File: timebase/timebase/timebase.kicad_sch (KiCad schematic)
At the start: 59 parts

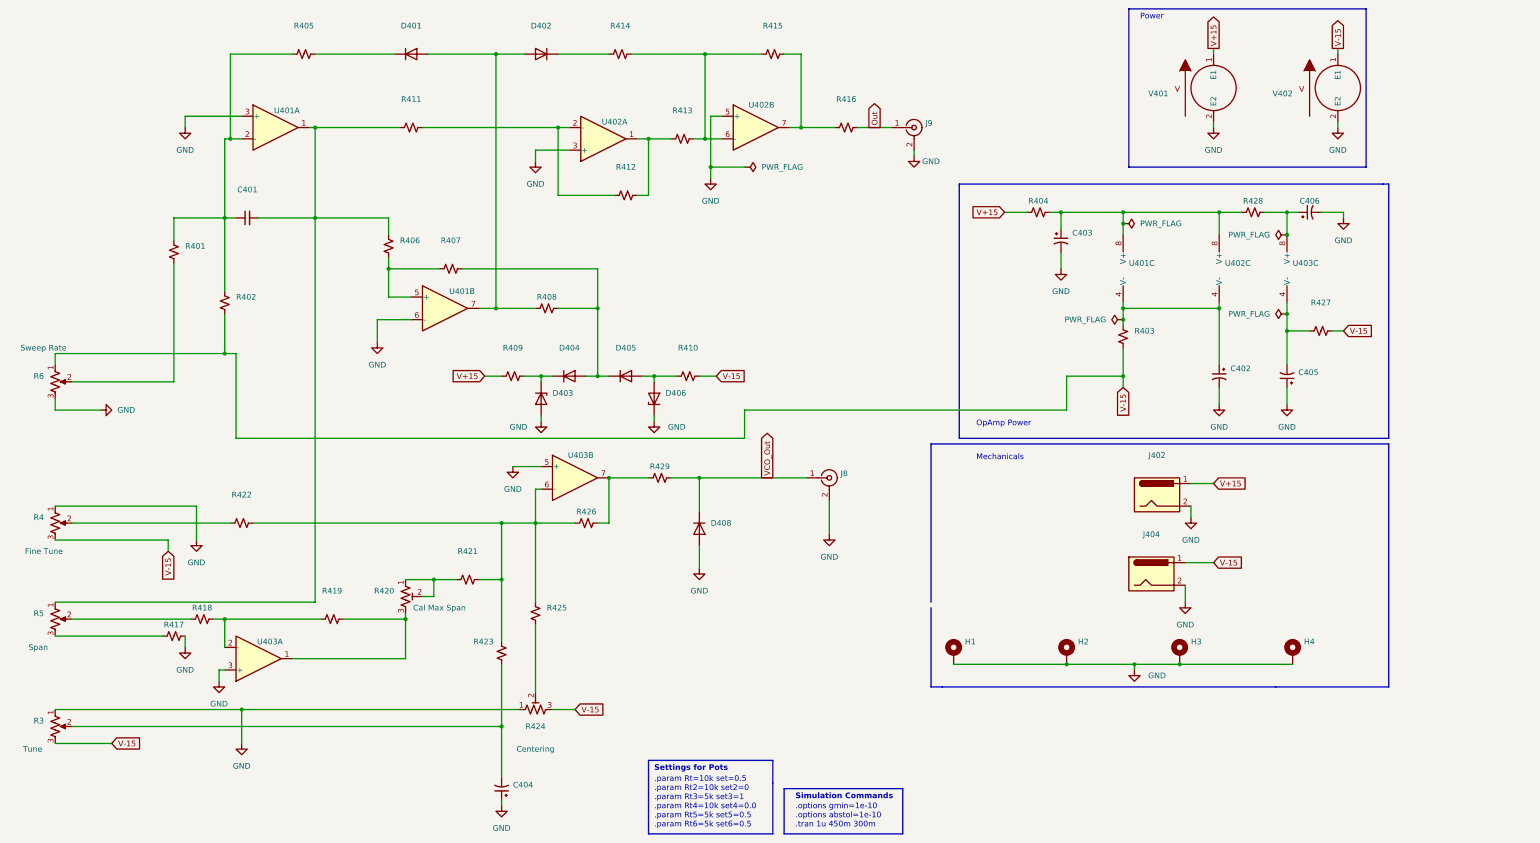
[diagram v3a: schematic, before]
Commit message: resolution-filters update
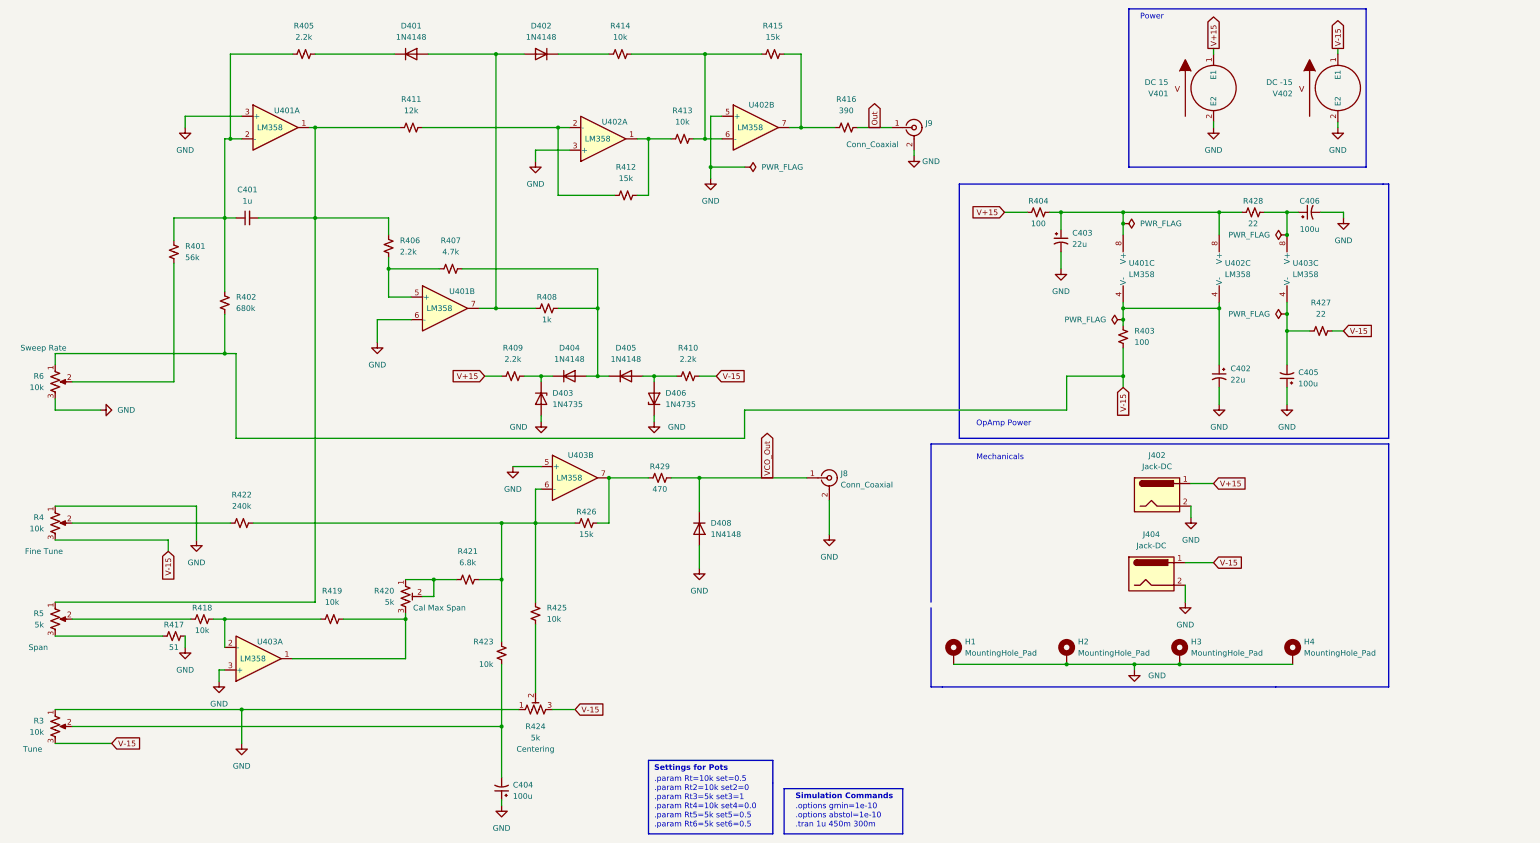
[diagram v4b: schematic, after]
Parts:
- C401: value (none) -> 1u; footprint (none) -> Capacitor_THT:C_Radial_D4.0mm_H5.0mm_P1.50mm
- C402, C403: value (none) -> 22u; footprint (none) -> Capacitor_THT:CP_Axial_L11.0mm_D6.0mm_P18.00mm_Horizontal
- C404, C405, C406: value (none) -> 100u; footprint (none) -> Capacitor_THT:CP_Axial_L11.0mm_D6.0mm_P18.00mm_Horizontal
- D401, D402, D404, D405, D408: value (none) -> 1N4148; footprint (none) -> Diode_THT:D_DO-35_SOD27_P7.62mm_Horizontal
- D403, D406: value (none) -> 1N4735; footprint (none) -> Diode_THT:D_DO-35_SOD27_P7.62mm_Horizontal
- H1, H2, H3, H4: value (none) -> MountingHole_Pad; footprint (none) -> MountingHole:MountingHole_2.7mm_M2.5_DIN965_Pad_TopOnly
- J402, J404: value (none) -> Jack-DC; footprint (none) -> timebase:CUI_PJ-007
- J8, J9: value (none) -> Conn_Coaxial; footprint (none) -> timebase:TE_5-1634503-1
- R3, R4, R6: value (none) -> 10k; footprint (none) -> Connector_Wire:SolderWire-0.127sqmm_1x03_P3.7mm_D0.48mm_OD1mm
- R401: value (none) -> 56k; footprint (none) -> Resistor_THT:R_Axial_DIN0207_L6.3mm_D2.5mm_P7.62mm_Horizontal
- R402: value (none) -> 680k; footprint (none) -> Resistor_THT:R_Axial_DIN0207_L6.3mm_D2.5mm_P7.62mm_Horizontal
- R403, R404: value (none) -> 100; footprint (none) -> Resistor_THT:R_Axial_DIN0207_L6.3mm_D2.5mm_P7.62mm_Horizontal
- R405, R406, R409, R410: value (none) -> 2.2k; footprint (none) -> Resistor_THT:R_Axial_DIN0207_L6.3mm_D2.5mm_P7.62mm_Horizontal
- R407: value (none) -> 4.7k; footprint (none) -> Resistor_THT:R_Axial_DIN0207_L6.3mm_D2.5mm_P7.62mm_Horizontal
- R408: value (none) -> 1k; footprint (none) -> Resistor_THT:R_Axial_DIN0207_L6.3mm_D2.5mm_P7.62mm_Horizontal
- R411: value (none) -> 12k; footprint (none) -> Resistor_THT:R_Axial_DIN0207_L6.3mm_D2.5mm_P7.62mm_Horizontal
- R412, R415, R426: value (none) -> 15k; footprint (none) -> Resistor_THT:R_Axial_DIN0207_L6.3mm_D2.5mm_P7.62mm_Horizontal
- R413, R414, R418, R419, R423, R425: value (none) -> 10k; footprint (none) -> Resistor_THT:R_Axial_DIN0207_L6.3mm_D2.5mm_P7.62mm_Horizontal
- R416: value (none) -> 390; footprint (none) -> Resistor_THT:R_Axial_DIN0207_L6.3mm_D2.5mm_P7.62mm_Horizontal
- R417: value (none) -> 51; footprint (none) -> Resistor_THT:R_Axial_DIN0207_L6.3mm_D2.5mm_P7.62mm_Horizontal
- R420, R424: value (none) -> 5k; footprint (none) -> Potentiometer_THT:Potentiometer_Bourns_3296W_Vertical
- R421: value (none) -> 6.8k; footprint (none) -> Resistor_THT:R_Axial_DIN0207_L6.3mm_D2.5mm_P7.62mm_Horizontal
- R422: value (none) -> 240k; footprint (none) -> Resistor_THT:R_Axial_DIN0207_L6.3mm_D2.5mm_P7.62mm_Horizontal
- R427, R428: value (none) -> 22; footprint (none) -> Resistor_THT:R_Axial_DIN0207_L6.3mm_D2.5mm_P7.62mm_Horizontal
- R429: value (none) -> 470; footprint (none) -> Resistor_THT:R_Axial_DIN0207_L6.3mm_D2.5mm_P7.62mm_Horizontal
- R5: value (none) -> 5k; footprint (none) -> Connector_Wire:SolderWire-0.127sqmm_1x03_P3.7mm_D0.48mm_OD1mm
- U401, U402, U403: value (none) -> LM358; footprint (none) -> timebase:DIP794W45P254L959H508Q8
- V401: value (none) -> DC 15; footprint (none) -> timebase:CUI_PJ-009A
- V402: value (none) -> DC -15; footprint (none) -> timebase:CUI_PJ-009A
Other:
- company: (none) -> Andy McCann KA3KAF and Doug McCann KA3KAG
- title: (none) -> Spectrum Analyzer: Timebase

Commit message: timebase updates
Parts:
- C401: footprint Capacitor_THT:C_Radial_D4.0mm_H5.0mm_P1.50mm -> Capacitor_THT:CP_Radial_D8.0mm_P3.50mm
- C402, C403, C404, C405, C406: footprint Capacitor_THT:CP_Axial_L11.0mm_D6.0mm_P18.00mm_Horizontal -> Capacitor_THT:CP_Radial_D8.0mm_P3.50mm
- H1, H2, H3, H4: footprint MountingHole:MountingHole_2.7mm_M2.5_DIN965_Pad_TopOnly -> MountingHole:MountingHole_3.2mm_M3
- J402, J404: footprint timebase:CUI_PJ-007 -> timebase:691137710002
- J8, J9: footprint timebase:TE_5-1634503-1 -> timebase:MOLEX_73391-0060
- R3, R4, R5, R6: footprint Connector_Wire:SolderWire-0.127sqmm_1x03_P3.7mm_D0.48mm_OD1mm -> Connector_Wire:SolderWire-0.25sqmm_1x03_P4.2mm_D0.65mm_OD1.7mm

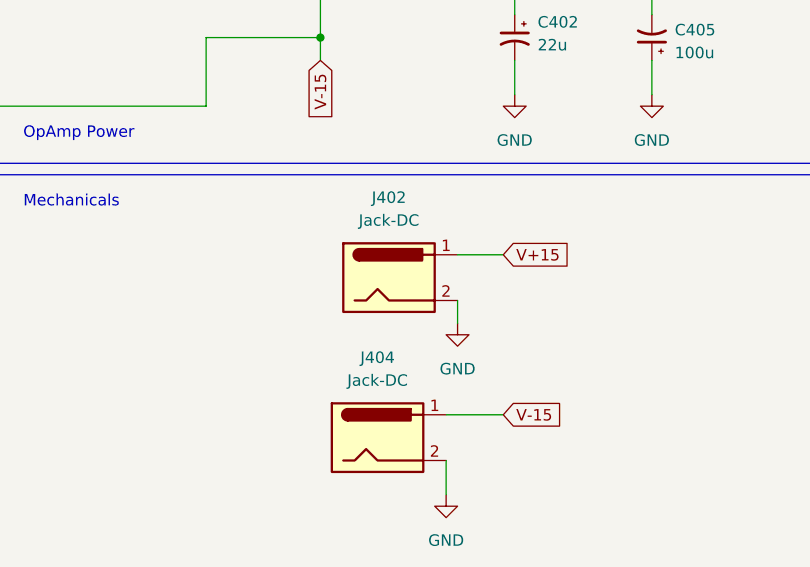
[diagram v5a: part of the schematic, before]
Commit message: some improvements to timebase and if log amp
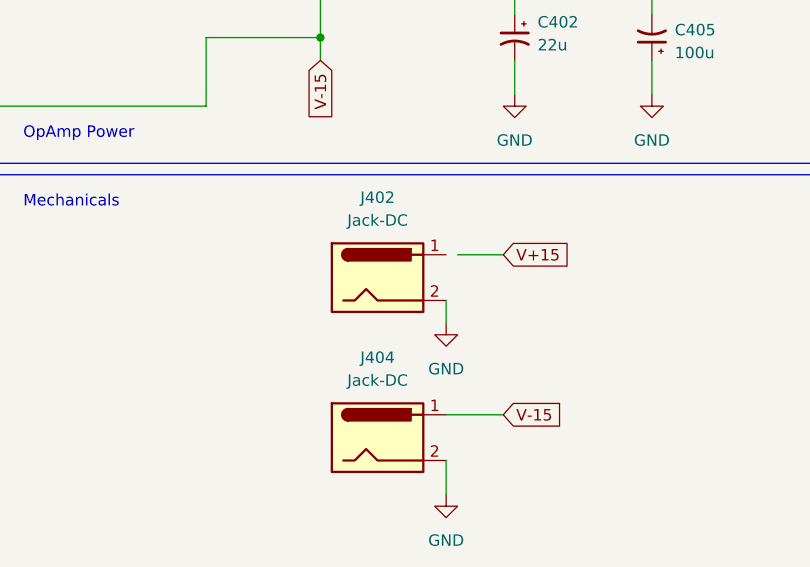
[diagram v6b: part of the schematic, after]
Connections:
- net V+15: no longer J402.1
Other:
- moved on the sheet: J402
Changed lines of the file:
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@@
     (stroke (width 0) (type default) (color 0 0 0 0))
   )
-  (wire (pts (xy 287.02 128.27) (xy 287.02 130.81))
+  (wire (pts (xy 285.75 128.27) (xy 285.75 130.81))
     (stroke (width 0) (type default) (color 0 0 0 0))
   )
@@
     (pin "1")
   )
-  (symbol (lib_id "power:GND") (at 287.02 130.81 0) (unit 1)
+  (symbol (lib_id "power:GND") (at 285.75 130.81 0) (unit 1)
     (in_bom yes) (on_board yes)
-    (property "Reference" "#PWR0420" (id 0) (at 287.02 137.16 0)
-      (effects (font (size 1.27 1.27)) hide)
-    )
-    (property "Value" "GND" (id 1) (at 287.02 135.89 0))
-    (property "Footprint" "" (id 2) (at 287.02 130.81 0)
-      (effects (font (size 1.27 1.27)) hide)
-    )
-    (property "Datasheet" "" (id 3) (at 287.02 130.81 0)
+    (property "Reference" "#PWR0420" (id 0) (at 285.75 137.16 0)
+      (effects (font (size 1.27 1.27)) hide)
+    )
+    (property "Value" "GND" (id 1) (at 285.75 135.89 0))
+    (property "Footprint" "" (id 2) (at 285.75 130.81 0)
+      (effects (font (size 1.27 1.27)) hide)
+    )
+    (property "Datasheet" "" (id 3) (at 285.75 130.81 0)
       (effects (font (size 1.27 1.27)) hide)
     )
@@
     (pin "1")
   )
-  (symbol (lib_id "Connector:Jack-DC") (at 279.4 125.73 0) (unit 1)
-    (in_bom yes) (on_board yes) (fields_autoplaced)
-    (property "Reference" "J402" (id 0) (at 279.4 116.84 0))
-    (property "Value" "Jack-DC" (id 1) (at 279.4 119.38 0))
-    (property "Footprint" "timebase:691137710002" (id 2) (at 280.67 126.746 0)
-      (effects (font (size 1.27 1.27)) hide)
-    )
-    (property "Datasheet" "~" (id 3) (at 280.67 126.746 0)
-      (effects (font (size 1.27 1.27)) hide)
-    )
-    (property "Spice_Primitive" "J" (id 4) (at 279.4 125.73 0)
-      (effects (font (size 1.27 1.27)) hide)
-    )
-    (property "Spice_Model" "Jack-DC" (id 5) (at 279.4 125.73 0)
-      (effects (font (size 1.27 1.27)) hide)
-    )
-    (property "Spice_Netlist_Enabled" "N" (id 6) (at 279.4 125.73 0)
-      (effects (font (size 1.27 1.27)) hide)
-    )
+  (symbol (lib_id "Connector:Jack-DC") (at 278.13 125.73 0) (unit 1)
+    (in_bom yes) (on_board yes) (fields_autoplaced)
+    (property "Reference" "J402" (id 0) (at 278.13 116.84 0))
+    (property "Value" "Jack-DC" (id 1) (at 278.13 119.38 0))
+    (property "Footprint" "timebase:691137710002" (id 2) (at 279.4 126.746 0)
+      (effects (font (size 1.27 1.27)) hide)
+    )
+    (property "Datasheet" "~" (id 3) (at 279.4 126.746 0)
+      (effects (font (size 1.27 1.27)) hide)
+    )
+    (property "Spice_Primitive" "J" (id 4) (at 278.13 125.73 0)
+      (effects (font (size 1.27 1.27)) hide)
+    )
+    (property "Spice_Model" "Jack-DC" (id 5) (at 278.13 125.73 0)
+      (effects (font (size 1.27 1.27)) hide)
+    )
+    (property "Spice_Netlist_Enabled" "N" (id 6) (at 278.13 125.73 0)
+      (effects (font (size 1.27 1.27)) hide)
+    )

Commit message: v7 conversion
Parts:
- D401, D402, D404, D405, D408: Spice_Lib_File timebase-spice\1N4148.mod -> (none); Spice_Model D1N4148 -> (none); Spice_Netlist_Enabled Y -> (none); Spice_Node_Sequence 2 1 -> (none); Spice_Primitive D -> (none)
- D403, D406: Spice_Lib_File timebase-spice\1N4735A.lib -> (none); Spice_Model DI_1N4735A -> (none); Spice_Netlist_Enabled Y -> (none); Spice_Node_Sequence 2 1 -> (none); Spice_Primitive X -> (none)
- H1, H2, H3, H4: value MountingHole_Pad -> ${SIM.PARAMS}; Spice_Netlist_Enabled N -> (none); Spice_Primitive R -> (none)
- J402, J404: Spice_Model Jack-DC -> (none); Spice_Netlist_Enabled N -> (none); Spice_Primitive J -> (none)
- J8, J9: Spice_Model Conn_Coaxial -> (none); Spice_Netlist_Enabled N -> (none); Spice_Primitive J -> (none)
- R3: Spice_Lib_File timebase-spice\Pot4.lib -> (none); Spice_Model pot_lin4 -> (none); Spice_Netlist_Enabled Y -> (none); Spice_Primitive X -> (none)
- R4: Spice_Lib_File timebase-spice\Pot2.lib -> (none); Spice_Model pot_lin2 -> (none); Spice_Netlist_Enabled Y -> (none); Spice_Primitive X -> (none)
- R420: Spice_Lib_File timebase-spice\Pot6.lib -> (none); Spice_Model pot_lin6 -> (none); Spice_Netlist_Enabled Y -> (none); Spice_Primitive X -> (none)
- R424: Spice_Lib_File timebase-spice\Pot5.lib -> (none); Spice_Model pot_lin5 -> (none); Spice_Netlist_Enabled Y -> (none); Spice_Primitive X -> (none)
- R5: Spice_Lib_File timebase-spice\Pot3.lib -> (none); Spice_Model pot_lin3 -> (none); Spice_Netlist_Enabled Y -> (none); Spice_Primitive X -> (none)
- R6: Spice_Lib_File timebase-spice\Pot.lib -> (none); Spice_Model pot_lin -> (none); Spice_Netlist_Enabled Y -> (none); Spice_Primitive X -> (none)
- U401, U402, U403: Spice_Lib_File timebase-spice\LM358-dual.lib -> (none); Spice_Model LM358c -> (none); Spice_Netlist_Enabled Y -> (none); Spice_Primitive X -> (none)
- V401: value DC 15 -> 15; Spice_Model dc 15 -> (none); Spice_Netlist_Enabled Y -> (none); Spice_Primitive V -> (none)
- V402: value DC -15 -> -15; Spice_Model dc -15 -> (none); Spice_Netlist_Enabled Y -> (none); Spice_Primitive V -> (none)

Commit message: Update to timebase and 2lo gerbers
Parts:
- C401: footprint Capacitor_THT:CP_Radial_D8.0mm_P3.50mm -> Capacitor_THT:C_Disc_D5.0mm_W2.5mm_P5.00mm
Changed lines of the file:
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@@
       (effects (font (size 1.27 1.27)))
     )
-    (property "Footprint" "Capacitor_THT:CP_Radial_D8.0mm_P3.50mm" (at 74.93 63.5 0)
+    (property "Footprint" "Capacitor_THT:C_Disc_D5.0mm_W2.5mm_P5.00mm" (at 74.93 63.5 0)
       (effects (font (size 1.27 1.27)) hide)
     )
